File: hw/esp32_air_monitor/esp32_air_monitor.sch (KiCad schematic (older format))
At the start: 7 parts, among them J1 Conn_01x02_Male, J2 Connector_LED_matrix_64x32, J3 Connector_LED_matrix_64x32, J4 Connector_Pimoroni_BME280, J5 Connector_Adafruit_VEML7700, U1 ESP32-DEVKITC-32D, U2 SCD30

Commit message: :)s
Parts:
- U2: footprint MODULE_SCD30 -> esp32_air_monitor:MODULE_SCD30
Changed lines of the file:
@@
 F 0 "U2" H 7550 5415 50  0000 C CNN
 F 1 "SCD30" H 7550 5324 50  0000 C CNN
-F 2 "MODULE_SCD30" H 7550 4750 50  0001 L BNN
+F 2 "esp32_air_monitor:MODULE_SCD30" H 7550 4750 50  0001 L BNN
 F 3 "" H 7550 4750 50  0001 L BNN
 F 4 "Manufacturer Recommendations" H 7550 4750 50  0001 L BNN "STANDARD"

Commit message: Update PCB
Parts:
- added R1, R2, R3, R4, R5, R6, R7: 10k, Resistor_SMD:R_1206_3216Metric_Pad1.30x1.75mm_HandSolder, symbol Device:R
- added SW1, SW2, SW3: SW_Push, qc_attiny:Push_Button_6x6mm, symbol Switch:SW_Push
- added SW4: SW_DIP_x04, Button_Switch_THT:SW_DIP_SPSTx04_Slide_9.78x12.34mm_W7.62mm_P2.54mm, symbol Switch:SW_DIP_x04
- U1: footprint MODULE_ESP32-DEVKITC-32D -> esp32_air_monitor:MODULE_ESP32-DEVKITC-32D
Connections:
- net labels added: BUT_1, BUT_2, BUT_3, DIP_1, DIP_2, DIP_3, DIP_4, R0
- net labels removed: B1
- wire segments 54 -> 86
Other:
- moved on the sheet: U2

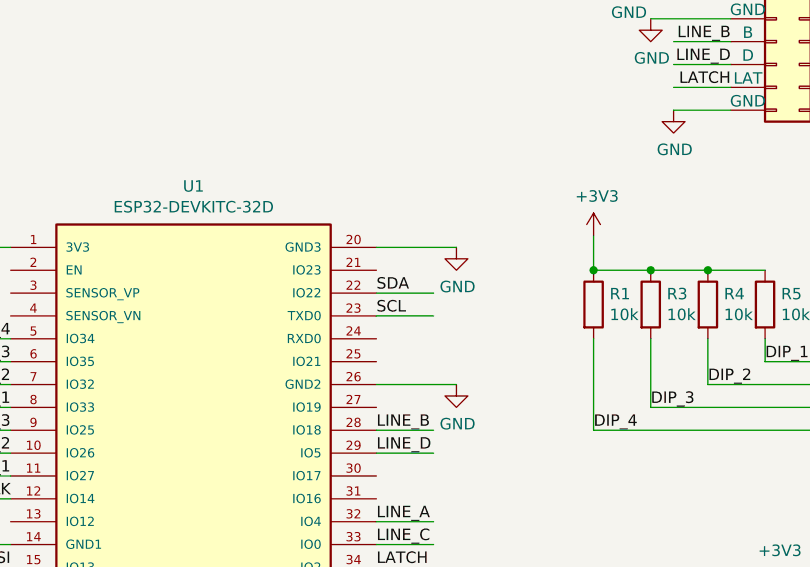
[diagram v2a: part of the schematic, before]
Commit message: Fix hardware bug (SCL pin), patch software for new hw revision
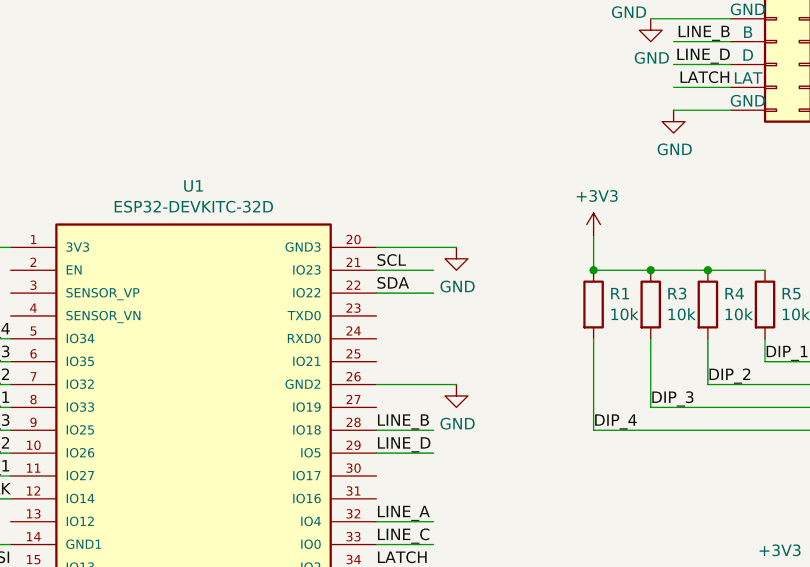
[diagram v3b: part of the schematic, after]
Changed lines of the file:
@@
 Wire Wire Line
 	4950 4500 4700 4500
-Text Label 4700 3400 0    50   ~ 0
+Text Label 4700 3200 0    50   ~ 0
 SCL
 Wire Wire Line
@@
 OE
 Wire Wire Line
-	4700 3400 4950 3400
+	4700 3200 4950 3200
 Text Label 4700 4500 0    50   ~ 0
 LATCH
